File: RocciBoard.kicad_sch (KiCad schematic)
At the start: 193 parts, among them J1 Battery, J10 M3, J11 I2C6, J12 Power, J13 M2, J14 I2C7, J2 I2C0, J3 I2C1, J4 I2C2, J5 I2C3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

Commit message: fixed #6 1k LCSL part number was wrong
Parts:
- Q1: LCSC C2997 -> C693103
- R16, R35, R36, R43, R44, R51, R52, R58, R59, R65: LCSC C1603 -> C21190
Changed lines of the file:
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@@
       (effects (font (size 1.27 1.27)) hide)
     )
-    (property "LCSC" "C1603" (at 364.998 230.4963 0)
+    (property "LCSC" "C21190" (at 364.998 230.4963 0)
       (effects (font (size 1.27 1.27)) hide)
     )
@@
       (effects (font (size 1.27 1.27)) hide)
     )
-    (property "LCSC" "C1603" (at 357.378 201.2863 0)
+    (property "LCSC" "C21190" (at 357.378 201.2863 0)
       (effects (font (size 1.27 1.27)) hide)
     )
@@
       (effects (font (size 1.27 1.27)) hide)
     )
-    (property "LCSC" "C1603" (at 364.998 170.8063 0)
+    (property "LCSC" "C21190" (at 364.998 170.8063 0)
       (effects (font (size 1.27 1.27)) hide)
     )
@@
       (effects (font (size 1.27 1.27)) (justify left) hide)
     )
-    (property "LCSC" "C2997" (at 269.24 71.12 0)
+    (property "LCSC" "C693103" (at 269.24 71.12 0)
       (effects (font (size 1.27 1.27)) hide)
     )
@@
       (effects (font (size 1.27 1.27)) hide)
     )
-    (property "LCSC" "C1603" (at 364.998 201.2863 0)
+    (property "LCSC" "C21190" (at 364.998 201.2863 0)
       (effects (font (size 1.27 1.27)) hide)
     )
@@
       (effects (font (size 1.27 1.27)) hide)
     )
-    (property "LCSC" "C1603" (at 357.378 170.8063 0)
+    (property "LCSC" "C21190" (at 357.378 170.8063 0)
       (effects (font (size 1.27 1.27)) hide)
     )
@@
       (effects (font (size 1.27 1.27)) hide)
     )
-    (property "LCSC" "C1603" (at 254.6263 88.392 0)
+    (property "LCSC" "C21190" (at 254.6263 88.392 0)
       (effects (font (size 1.27 1.27)) hide)
     )
@@
       (effects (font (size 1.27 1.27)) hide)
     )
-    (property "LCSC" "C1603" (at 357.378 141.5963 0)
+    (property "LCSC" "C21190" (at 357.378 141.5963 0)
       (effects (font (size 1.27 1.27)) hide)
     )
@@
       (effects (font (size 1.27 1.27)) hide)
     )
-    (property "LCSC" "C1603" (at 283.718 83.1763 0)
+    (property "LCSC" "C21190" (at 283.718 83.1763 0)
       (effects (font (size 1.27 1.27)) hide)
     )
@@
       (effects (font (size 1.27 1.27)) hide)
     )
-    (property "LCSC" "C1603" (at 364.998 141.5963 0)
+    (property "LCSC" "C21190" (at 364.998 141.5963 0)
       (effects (font (size 1.27 1.27)) hide)
     )
@@
       (effects (font (size 1.27 1.27)) hide)
     )
-    (property "LCSC" "C1603" (at 357.378 230.4963 0)
+    (property "LCSC" "C21190" (at 357.378 230.4963 0)
       (effects (font (size 1.27 1.27)) hide)
     )

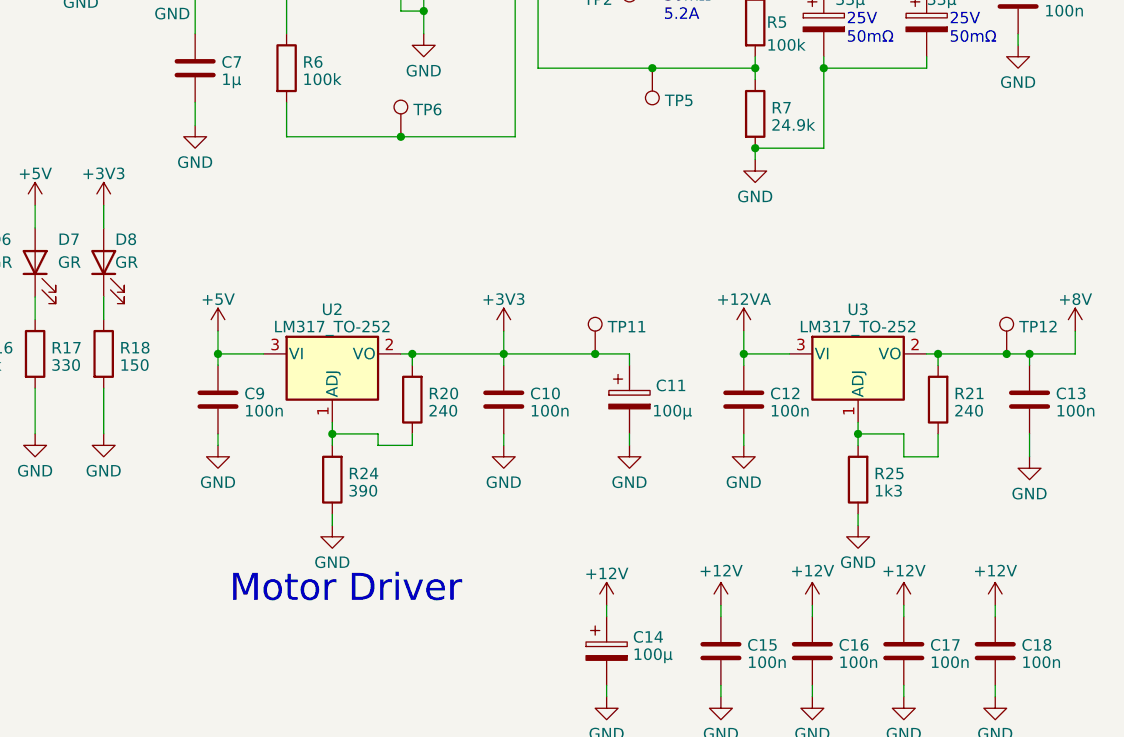
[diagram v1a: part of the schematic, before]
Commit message: fix #8 prevent backcurrent from Arduino USB
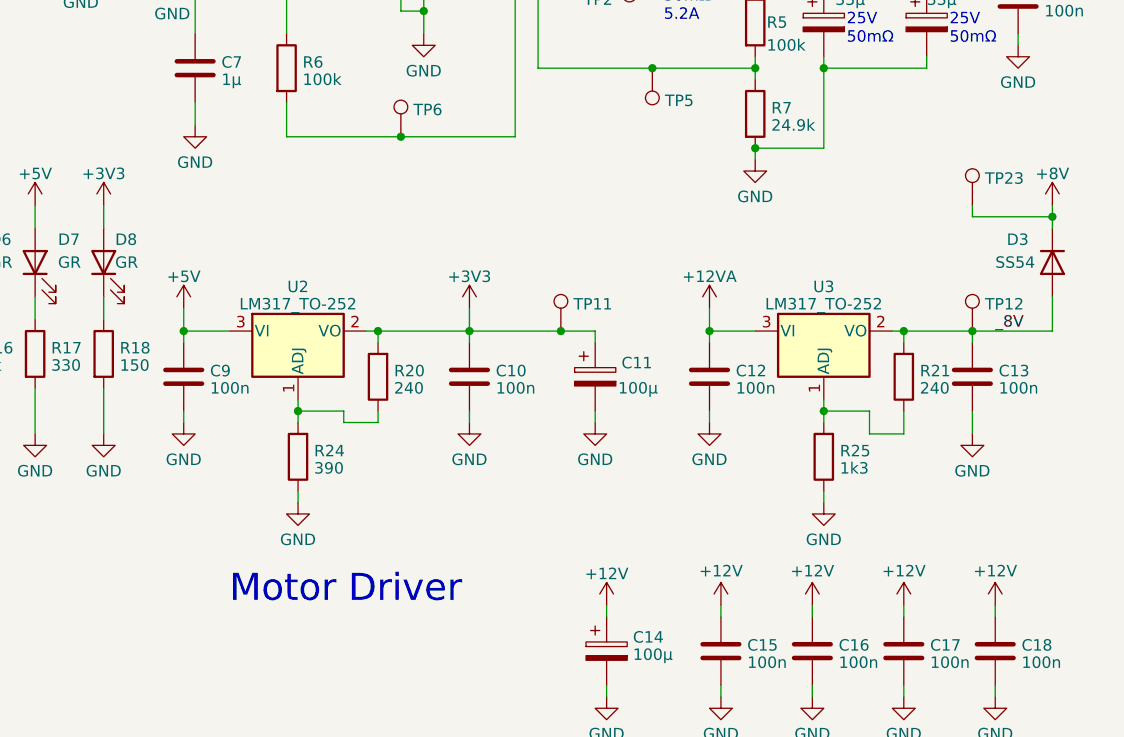
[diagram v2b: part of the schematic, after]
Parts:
- added D3: SS54, Diode_SMD:D_SMA, symbol Diode:1N5400
- added TP23: ~, TestPoint:TestPoint_Pad_D1.0mm, symbol Connector:TestPoint
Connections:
- net +8V: now also D3.1 (K), TP23.1; no longer C13.1, R21.2, TP12.1, U3.2 (VO)
- new net _8V: C13.1, D3.2 (A), R21.2, TP12.1, U3.2 (VO)
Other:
- moved on the sheet: C10, C11, C12, C13, C9, R20, R21, R24, R25, TP11, TP12, U2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

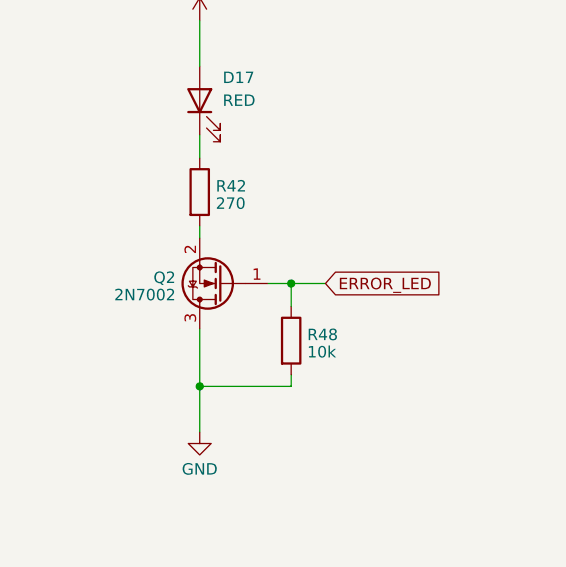
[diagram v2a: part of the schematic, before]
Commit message: fix #5  Error LED Q2 Source<->Drain vertauscht
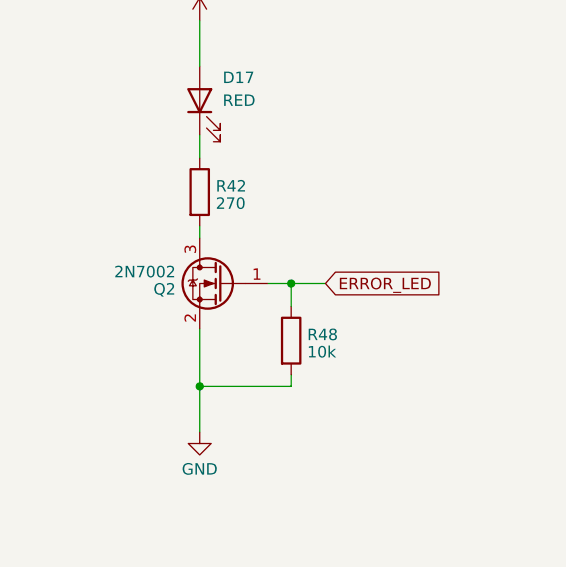
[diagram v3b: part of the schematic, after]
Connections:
- net GND: now also Q2.2 (S); no longer Q2.3 (D)
- net at R42.2: now also Q2.3 (D); no longer Q2.2 (S)
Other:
- moved on the sheet: Q2
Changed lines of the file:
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@@
     )
   )
-  (symbol (lib_id "Device:Q_NMOS_GSD") (at 38.1 180.34 180) (unit 1)
-    (in_bom yes) (on_board yes) (dnp no) (fields_autoplaced)
-    (property "Reference" "Q2" (at 32.893 179.6963 0)
+  (symbol (lib_id "Device:Q_NMOS_GSD") (at 38.1 180.34 0) (mirror y) (unit 1)
+    (in_bom yes) (on_board yes) (dnp no)
+    (property "Reference" "Q2" (at 32.893 180.9837 0)
       (effects (font (size 1.27 1.27)) (justify left))
     )
-    (property "Value" "2N7002" (at 32.893 181.6173 0)
+    (property "Value" "2N7002" (at 32.893 179.0627 0)
       (effects (font (size 1.27 1.27)) (justify left))
     )
-    (property "Footprint" "Package_TO_SOT_SMD:SOT-23" (at 33.02 182.88 0)
+    (property "Footprint" "Package_TO_SOT_SMD:SOT-23" (at 33.02 177.8 0)
       (effects (font (size 1.27 1.27)) hide)
     )
@@
       (effects (font (size 1.27 1.27)) hide)
     )
-    (property "LCSC" "C8545" (at 32.893 179.6963 0)
+    (property "LCSC" "C8545" (at 32.893 180.9837 0)
       (effects (font (size 1.27 1.27)) hide)
     )

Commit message: fix #7 all status LEDs are too bright
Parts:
- R16, R35, R36, R43, R44, R51, R52, R58, R59: value 1k -> 2k; LCSC C21190 -> C22975
- R17: value 330 -> 620; LCSC C23138 -> C23228
- R18: value 150 -> 330; LCSC C22808 -> C23138
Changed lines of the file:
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@@
       (effects (font (size 1.27 1.27)) (justify left))
     )
-    (property "Value" "1k" (at 364.998 232.4173 0)
+    (property "Value" "2k" (at 364.998 232.4173 0)
       (effects (font (size 1.27 1.27)) (justify left))
     )
@@
       (effects (font (size 1.27 1.27)) hide)
     )
-    (property "LCSC" "C21190" (at 364.998 230.4963 0)
+    (property "LCSC" "C22975" (at 364.998 230.4963 0)
       (effects (font (size 1.27 1.27)) hide)
     )
@@
       (effects (font (size 1.27 1.27)) (justify left))
     )
-    (property "Value" "330" (at 291.338 85.0973 0)
+    (property "Value" "620" (at 291.338 85.0973 0)
       (effects (font (size 1.27 1.27)) (justify left))
     )
@@
       (effects (font (size 1.27 1.27)) hide)
     )
-    (property "LCSC" "C23138" (at 291.338 83.1763 0)
+    (property "LCSC" "C23228" (at 291.338 83.1763 0)
       (effects (font (size 1.27 1.27)) hide)
     )
@@
       (effects (font (size 1.27 1.27)) (justify left))
     )
-    (property "Value" "1k" (at 357.378 203.2073 0)
+    (property "Value" "2k" (at 357.378 203.2073 0)
       (effects (font (size 1.27 1.27)) (justify left))
     )
@@
       (effects (font (size 1.27 1.27)) hide)
     )
-    (property "LCSC" "C21190" (at 357.378 201.2863 0)
+    (property "LCSC" "C22975" (at 357.378 201.2863 0)
       (effects (font (size 1.27 1.27)) hide)
     )
@@
       (effects (font (size 1.27 1.27)) (justify left))
     )
-    (property "Value" "150" (at 298.958 85.0973 0)
+    (property "Value" "330" (at 298.958 85.0973 0)
       (effects (font (size 1.27 1.27)) (justify left))
     )
@@
       (effects (font (size 1.27 1.27)) hide)
     )
-    (property "LCSC" "C22808" (at 298.958 83.1763 0)
+    (property "LCSC" "C23138" (at 298.958 83.1763 0)
       (effects (font (size 1.27 1.27)) hide)
     )
@@
       (effects (font (size 1.27 1.27)) (justify left))
     )
-    (property "Value" "1k" (at 364.998 172.7273 0)
+    (property "Value" "2k" (at 364.998 172.7273 0)
       (effects (font (size 1.27 1.27)) (justify left))
     )
@@
       (effects (font (size 1.27 1.27)) hide)
     )
-    (property "LCSC" "C21190" (at 364.998 170.8063 0)
+    (property "LCSC" "C22975" (at 364.998 170.8063 0)
       (effects (font (size 1.27 1.27)) hide)
     )
@@
       (effects (font (size 1.27 1.27)) (justify left))
     )
-    (property "Value" "1k" (at 364.998 203.2073 0)
+    (property "Value" "2k" (at 364.998 203.2073 0)
       (effects (font (size 1.27 1.27)) (justify left))
     )
@@
       (effects (font (size 1.27 1.27)) hide)
     )
-    (property "LCSC" "C21190" (at 364.998 201.2863 0)
+    (property "LCSC" "C22975" (at 364.998 201.2863 0)
       (effects (font (size 1.27 1.27)) hide)
     )
@@
       (effects (font (size 1.27 1.27)) (justify left))
     )
-    (property "Value" "1k" (at 357.378 172.7273 0)
+    (property "Value" "2k" (at 357.378 172.7273 0)
       (effects (font (size 1.27 1.27)) (justify left))
     )
@@
       (effects (font (size 1.27 1.27)) hide)
     )
-    (property "LCSC" "C21190" (at 357.378 170.8063 0)
+    (property "LCSC" "C22975" (at 357.378 170.8063 0)
       (effects (font (size 1.27 1.27)) hide)
     )
@@
       (effects (font (size 1.27 1.27)) (justify left))
     )
-    (property "Value" "1k" (at 357.378 143.5173 0)
+    (property "Value" "2k" (at 357.378 143.5173 0)
       (effects (font (size 1.27 1.27)) (justify left))
     )
@@
       (effects (font (size 1.27 1.27)) hide)
     )
-    (property "LCSC" "C21190" (at 357.378 141.5963 0)
+    (property "LCSC" "C22975" (at 357.378 141.5963 0)
       (effects (font (size 1.27 1.27)) hide)
     )
@@
       (effects (font (size 1.27 1.27)) (justify left))
     )
-    (property "Value" "1k" (at 283.718 85.0973 0)
+    (property "Value" "2k" (at 283.718 85.0973 0)
       (effects (font (size 1.27 1.27)) (justify left))
     )
@@
       (effects (font (size 1.27 1.27)) hide)
     )
-    (property "LCSC" "C21190" (at 283.718 83.1763 0)
+    (property "LCSC" "C22975" (at 283.718 83.1763 0)
       (effects (font (size 1.27 1.27)) hide)
     )
@@
       (effects (font (size 1.27 1.27)) (justify left))
     )
-    (property "Value" "1k" (at 364.998 143.5173 0)
+    (property "Value" "2k" (at 364.998 143.5173 0)
       (effects (font (size 1.27 1.27)) (justify left))
     )
@@
       (effects (font (size 1.27 1.27)) hide)
     )
-    (property "LCSC" "C21190" (at 364.998 141.5963 0)
+    (property "LCSC" "C22975" (at 364.998 141.5963 0)
       (effects (font (size 1.27 1.27)) hide)
     )
@@
       (effects (font (size 1.27 1.27)) (justify left))
     )
-    (property "Value" "1k" (at 357.378 232.4173 0)
+    (property "Value" "2k" (at 357.378 232.4173 0)
       (effects (font (size 1.27 1.27)) (justify left))
     )
@@
       (effects (font (size 1.27 1.27)) hide)
     )
-    (property "LCSC" "C21190" (at 357.378 230.4963 0)
+    (property "LCSC" "C22975" (at 357.378 230.4963 0)
       (effects (font (size 1.27 1.27)) hide)
     )

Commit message: fix  #9 OVP 12V<->5V short circuit protection
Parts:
- removed D26: 3V4, Diode_SMD:D_MiniMELF, symbol Device:D_Zener
- removed D27: 5V1, Diode_SMD:D_MiniMELF, symbol Device:D_Zener
- added D33: BT137S-600E, Package_TO_SOT_SMD:TO-252-2, symbol Device:Q_TRIAC_A1A2G
- added R68, R71: 1k, Resistor_SMD:R_0603_1608Metric, symbol Device:R
- added R69: 1k5, Resistor_SMD:R_0603_1608Metric, symbol Device:R
- added R70: 1k3, Resistor_SMD:R_0603_1608Metric, symbol Device:R
- added R72: 2k, Resistor_SMD:R_0603_1608Metric, symbol Device:R
- added U11, U12: CJ431, Package_TO_SOT_SMD:SOT-23, symbol Reference_Voltage:TL432DBZ
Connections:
- net +12VA: now also D33.1 (A1), R68.1
- net +3V3: now also R70.1
- net +5V: now also R69.1
- net GND: now also D33.2 (A2), R71.2, R72.2, U11.3 (A), U12.3 (A)
- new net: R69.2, R71.1, U11.1 (REF)
- new net: D33.3 (G), R68.2, U11.2 (K), U12.2 (K)
- new net: R70.2, R72.1, U12.1 (REF)
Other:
- moved on the sheet: D17, F11, F9, J12, Q2, R42, R48

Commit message: V 1.1
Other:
- note added: "fix #9 OVP 12V<->5V short circuit protection fix #7 all status LEDs are too bright fix #5 Error LED Q2 Source<->Drain vertauscht fix #8 prevent backcurrent from Arduino USB fix #6 1k LCSL part number was wrong"
- note added: "since 1.0:"
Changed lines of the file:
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@@
   (title_block
     (title "RoCCI Shield")
-    (date "2023-07-29")
-    (rev "1.0")
+    (date "2023-09-30")
+    (rev "1.1")
     (company "RoCCI e.V.")
   )
@@
     (effects (font (size 3 3)) (justify left bottom))
   )
+  (text "since 1.0:" (at 307.34 255.27 0)
+    (effects (font (size 1.27 1.27) (thickness 0.254) bold) (justify left bottom))
+  )
   (text "50V\n340mΩ" (at 295.91 40.64 0)
     (effects (font (size 1.27 1.27) (color 0 132 0 1)) (justify left bottom))
@@
     (effects (font (size 1.27 1.27)) (justify left bottom))
   )
+  (text "fix #9 OVP 12V<->5V short circuit protection\nfix #7 all status LEDs are too bright\nfix #5 Error LED Q2 Source<->Drain vertauscht\nfix #8 prevent backcurrent from Arduino USB\nfix #6 1k LCSL part number was wrong "
+    (at 318.77 265.43 0)
+    (effects (font (size 1.27 1.27)) (justify left bottom))
+  )

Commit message: fix #13 #12 #11 #10
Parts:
- added JP12: Jumper_2_Bridged, Jumper:SolderJumper-2_P1.3mm_Open_Pad1.0x1.5mm, symbol Jumper:Jumper_2_Bridged
- added SW1: SW_DIP_x01, Button_Switch_SMD:SW_Push_1P1T_XKB_TS-1187A, symbol Switch:SW_DIP_x01
- D33, R68: now not fitted
- Q1: value IRF7404 -> IRF 7424; LCSC C693103 -> C148149
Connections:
- net +12VA: now also C14.1, C15.1, C16.1, C17.1, C18.1, U6.5 (VM), U7.5 (VM), U8.5 (VM), U9.5 (VM)
- net GND: now also SW1.1
- net SHUTOFF: now reaches R19.2, R26.1, TP14.1, U4.4 (INB-)
- net SHUTOFF: now also JP12.1 (A)
- net at D33.3 (G), R68.2, U11.2 (K)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: now also JP12.2 (B)
- net at XA1.RST1 (RESET): now also SW1.2
- net +12V renamed 12V_after_fuse
- net 12V_after_fuse: no longer C14.1, C15.1, C16.1, C17.1, C18.1, U6.5 (VM), U7.5 (VM), U8.5 (VM), U9.5 (VM)
- no-connect marks 65 -> 64
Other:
- note added: "fix #9 OVP 12V<->5V short circuit protection fix #7 all status LEDs are too bright fix #5 Error LED Q2 Source<->Drain vertauscht fix #8 prevent backcurrent from Arduino USB fix #6 1k LCSL part number was wrong fix #10 change motor supply after mosfet and added 11 A P-Channel mosfet"
- note removed: "fix #9 OVP 12V<->5V short circuit protection fix #7 all status LEDs are too bright fix #5 Error LED Q2 Source<->Drain vertauscht fix #8 prevent backcurrent from Arduino USB fix #6 1k LCSL part number was wrong"
